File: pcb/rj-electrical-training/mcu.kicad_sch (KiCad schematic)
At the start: 29 parts, among them SW1 PTS810, SW2 PTS810, U1 RP2040, U2 W25Q16JVSS, Y1 ABM8-272-T3

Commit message: Added SPI buses so slave master protocols work
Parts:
- added J3, J4: Conn_01x06, Connector_JST:JST_PH_S6B-PH-K_1x06_P2.00mm_Horizontal, symbol Connector_Generic:Conn_01x06
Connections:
- net +3.3V: now also J3.2 (Pin_2), J4.2 (Pin_2)
- net GND: now also J3.1 (Pin_1), J4.1 (Pin_1)
- net QSPI_SD0: no longer U1.53 (QSPI_SD0)
- net slave_rx: now reaches U1.11 (GPIO8)
- net slave_rx: now also J3.4 (Pin_4)
- net slave_csn: now reaches U1.12 (GPIO9)
- net slave_csn: now also J3.5 (Pin_5)
- net slace_sck: now reaches U1.13 (GPIO10)
- net slave_tx: now reaches U1.14 (GPIO11)
- net slave_tx: now also J3.3 (Pin_3)
- net master_rx: now reaches U1.6 (GPIO4)
- net master_rx: now also J4.4 (Pin_4)
- net master_csn: now reaches U1.7 (GPIO5)
- net master_csn: now also J4.5 (Pin_5)
- net master_sck: now reaches U1.8 (GPIO6)
- net master_sck: now also J4.6 (Pin_6)
- net master_tx: now reaches U1.9 (GPIO7)
- net master_tx: now also J4.3 (Pin_3)
- new net slave_sck: J3.6 (Pin_6)
- no-connect marks 17 -> 9
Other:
- note added: "SPI Connectors"

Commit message: Integrated LEDs to circuit
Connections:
- net ind_led0: no longer names the net of U1.30 (GPIO19)
- net ind_led1: no longer names the net of U1.31 (GPIO20)
- net ind_led2: no longer names the net of U1.32 (GPIO21)
- net ind_led3: no longer names the net of U1.34 (GPIO22)
- net ind_led4: no longer names the net of U1.35 (GPIO23)
- net ind_led5: no longer names the net of U1.36 (GPIO24)
- net ind_led6: no longer names the net of U1.37 (GPIO25)
- no-connect marks 9 -> 16

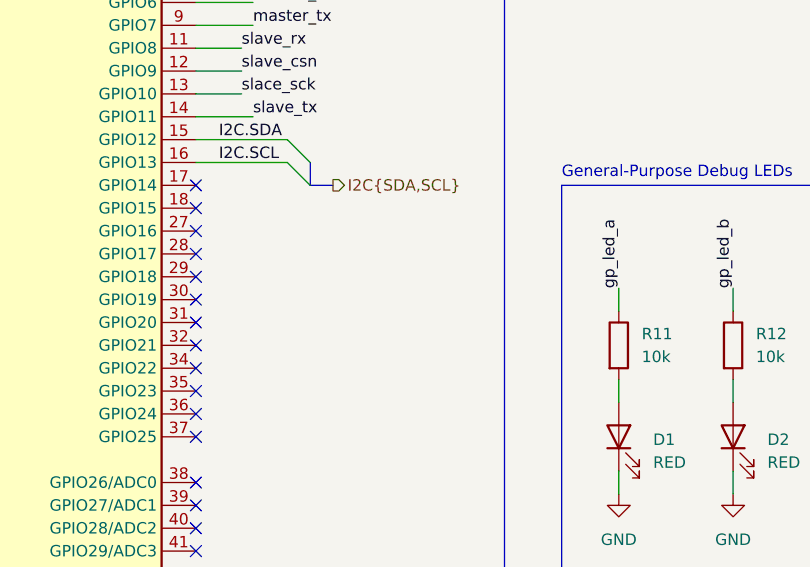
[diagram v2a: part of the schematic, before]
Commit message: Separate SDA SCL
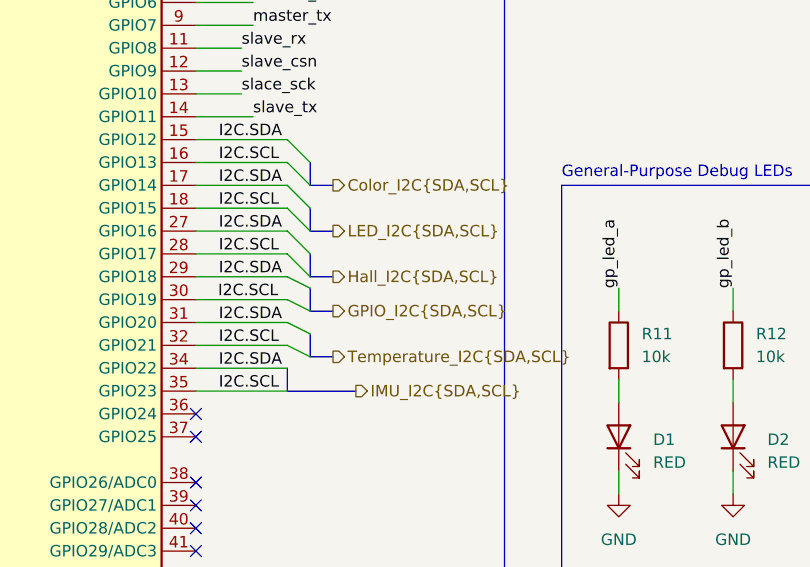
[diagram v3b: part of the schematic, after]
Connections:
- net I2C.SCL: now also U1.18 (GPIO15), U1.28 (GPIO17), U1.30 (GPIO19), U1.32 (GPIO21), U1.35 (GPIO23)
- net I2C.SDA: now also U1.17 (GPIO14), U1.27 (GPIO16), U1.29 (GPIO18), U1.31 (GPIO20), U1.34 (GPIO22)
- no-connect marks 16 -> 6
